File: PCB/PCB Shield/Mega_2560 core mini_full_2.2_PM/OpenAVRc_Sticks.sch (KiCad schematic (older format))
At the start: 58 parts, among them P11 Trim, P12 Stick_left, P13 Stick_right, P14 Switch, P23 Rot_1, P24 Rot_2, P25 Keys, P28 5v/3,3v manches, P31 Pot2, P32 Pot1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

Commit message: Update Shield v2.2
-Add pullup on Rx core
-Add 3D views TOP and BOTTOM
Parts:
- P12: footprint Pin_Headers:Pin_Header_Straight_2x03_Pitch2.54mm -> Mylib_v2.2:Pin_Header_Straight_2x03_Pitch2.54mm
- P13: footprint Pin_Headers:Pin_Header_Straight_1x06_Pitch2.54mm -> Mylib_v2.2:Pin_Header_Straight_2x03_Pitch2.54mm
- R11, R12, R13, R14, R24, R25, R26, R28, R29, R31, R32, R34, R35, R37: footprint Resistors_SMD:R_1206 -> Mylib_v2.2:R_1206
- U6: footprint Librairie master:SOP14 -> Mylib_v2.2:SOP14
- W1, W2, W3, W4: footprint anthoperso:TESTPT -> Mylib_v2.2:TESTPT
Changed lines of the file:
@@
 F 0 "U6" H 6100 4700 50  0000 L CNN
 F 1 "MCP6004" H 6100 4300 50  0000 L CNN
-F 2 "Librairie master:SOP14" H 6050 4600 50  0001 C CNN
+F 2 "Mylib_v2.2:SOP14" H 6050 4600 50  0001 C CNN
 F 3 "" H 6150 4700 50  0000 C CNN
 	2    6100 4500
@@
 F 0 "U6" H 9500 4750 50  0000 L CNN
 F 1 "MCP6004" H 9500 4350 50  0000 L CNN
-F 2 "Librairie master:SOP14" H 9450 4650 50  0001 C CNN
+F 2 "Mylib_v2.2:SOP14" H 9450 4650 50  0001 C CNN
 F 3 "" H 9550 4750 50  0000 C CNN
 	4    9500 4550
@@
 F 0 "U6" H 7800 4700 50  0000 L CNN
 F 1 "MCP6004" H 7800 4300 50  0000 L CNN
-F 2 "Librairie master:SOP14" H 7750 4600 50  0001 C CNN
+F 2 "Mylib_v2.2:SOP14" H 7750 4600 50  0001 C CNN
 F 3 "" H 7850 4700 50  0000 C CNN
 	3    7800 4500
@@
 F 0 "U6" H 4400 4700 50  0000 L CNN
 F 1 "MCP6004" H 4400 4300 50  0000 L CNN
-F 2 "Librairie master:SOP14" H 4350 4600 50  0001 C CNN
+F 2 "Mylib_v2.2:SOP14" H 4350 4600 50  0001 C CNN
 F 3 "" H 4450 4700 50  0000 C CNN
 	1    4400 4500
@@
 F 0 "R26" V 5030 5350 50  0000 C CNN
 F 1 "47K" V 4950 5350 50  0000 C CNN
-F 2 "Resistors_SMD:R_1206" V 4880 5350 50  0001 C CNN
+F 2 "Mylib_v2.2:R_1206" V 4880 5350 50  0001 C CNN
 F 3 "" H 4950 5350 50  0000 C CNN
 	1    4950 5350
@@
 F 0 "R28" V 5230 5350 50  0000 C CNN
 F 1 "120K" V 5150 5350 50  0000 C CNN
-F 2 "Resistors_SMD:R_1206" V 5080 5350 50  0001 C CNN
+F 2 "Mylib_v2.2:R_1206" V 5080 5350 50  0001 C CNN
 F 3 "" H 5150 5350 50  0000 C CNN
 	1    5150 5350
@@
 F 0 "R29" V 6730 5350 50  0000 C CNN
 F 1 "47K" V 6650 5350 50  0000 C CNN
-F 2 "Resistors_SMD:R_1206" V 6580 5350 50  0001 C CNN
+F 2 "Mylib_v2.2:R_1206" V 6580 5350 50  0001 C CNN
 F 3 "" H 6650 5350 50  0000 C CNN
 	1    6650 5350
@@
 F 0 "R31" V 6930 5350 50  0000 C CNN
 F 1 "120K" V 6850 5350 50  0000 C CNN
-F 2 "Resistors_SMD:R_1206" V 6780 5350 50  0001 C CNN
+F 2 "Mylib_v2.2:R_1206" V 6780 5350 50  0001 C CNN
 F 3 "" H 6850 5350 50  0000 C CNN
 	1    6850 5350
@@
 F 0 "R32" V 8430 5350 50  0000 C CNN
 F 1 "47K" V 8350 5350 50  0000 C CNN
-F 2 "Resistors_SMD:R_1206" V 8280 5350 50  0001 C CNN
+F 2 "Mylib_v2.2:R_1206" V 8280 5350 50  0001 C CNN
 F 3 "" H 8350 5350 50  0000 C CNN
 	1    8350 5350
@@
 F 0 "R34" V 8630 5350 50  0000 C CNN
 F 1 "120K" V 8550 5350 50  0000 C CNN
-F 2 "Resistors_SMD:R_1206" V 8480 5350 50  0001 C CNN
+F 2 "Mylib_v2.2:R_1206" V 8480 5350 50  0001 C CNN
 F 3 "" H 8550 5350 50  0000 C CNN
 	1    8550 5350
@@
 F 0 "R35" V 10130 5400 50  0000 C CNN
 F 1 "47K" V 10050 5400 50  0000 C CNN
-F 2 "Resistors_SMD:R_1206" V 9980 5400 50  0001 C CNN
+F 2 "Mylib_v2.2:R_1206" V 9980 5400 50  0001 C CNN
 F 3 "" H 10050 5400 50  0000 C CNN
 	1    10050 5400
@@
 F 0 "R37" V 10330 5400 50  0000 C CNN
 F 1 "120K" V 10250 5400 50  0000 C CNN
-F 2 "Resistors_SMD:R_1206" V 10180 5400 50  0001 C CNN
+F 2 "Mylib_v2.2:R_1206" V 10180 5400 50  0001 C CNN
 F 3 "" H 10250 5400 50  0000 C CNN
 	1    10250 5400
@@
 F 0 "R24" V 3630 5550 50  0000 C CNN
 F 1 "39K" V 3550 5550 50  0000 C CNN
-F 2 "Resistors_SMD:R_1206" V 3480 5550 50  0001 C CNN
+F 2 "Mylib_v2.2:R_1206" V 3480 5550 50  0001 C CNN
 F 3 "" H 3550 5550 50  0000 C CNN
 	1    3550 5550
@@
 F 0 "R25" V 4080 5250 50  0000 C CNN
 F 1 "39K" V 4000 5250 50  0000 C CNN
-F 2 "Resistors_SMD:R_1206" V 3930 5250 50  0001 C CNN
+F 2 "Mylib_v2.2:R_1206" V 3930 5250 50  0001 C CNN
 F 3 "" H 4000 5250 50  0000 C CNN
 	1    4000 5250
@@
 F 0 "W1" H 4900 4660 50  0000 C CNN
 F 1 "TEST_2P" H 4900 4530 50  0000 C CNN
-F 2 "anthoperso:TESTPT" H 4900 4600 50  0001 C CNN
+F 2 "Mylib_v2.2:TESTPT" H 4900 4600 50  0001 C CNN
 F 3 "" H 4900 4600 50  0000 C CNN
 	1    4900 4600
@@
 F 0 "W2" H 6600 4660 50  0000 C CNN
 F 1 "TEST_2P" H 6600 4530 50  0000 C CNN
-F 2 "anthoperso:TESTPT" H 6600 4600 50  0001 C CNN
+F 2 "Mylib_v2.2:TESTPT" H 6600 4600 50  0001 C CNN
 F 3 "" H 6600 4600 50  0000 C CNN
 	1    6600 4600
@@
 F 0 "W3" H 8300 4660 50  0000 C CNN
 F 1 "TEST_2P" H 8300 4530 50  0000 C CNN
-F 2 "anthoperso:TESTPT" H 8300 4600 50  0001 C CNN
+F 2 "Mylib_v2.2:TESTPT" H 8300 4600 50  0001 C CNN
 F 3 "" H 8300 4600 50  0000 C CNN
 	1    8300 4600
@@
 F 0 "W4" H 10000 4710 50  0000 C CNN
 F 1 "TEST_2P" H 10000 4580 50  0000 C CNN
-F 2 "anthoperso:TESTPT" H 10000 4650 50  0001 C CNN
+F 2 "Mylib_v2.2:TESTPT" H 10000 4650 50  0001 C CNN
 F 3 "" H 10000 4650 50  0000 C CNN
 	1    10000 4650
@@
 F 0 "R11" V 5230 4800 50  0000 C CNN
 F 1 "68K" V 5150 4800 50  0000 C CNN
-F 2 "Resistors_SMD:R_1206" V 5080 4800 50  0001 C CNN
+F 2 "Mylib_v2.2:R_1206" V 5080 4800 50  0001 C CNN
 F 3 "" H 5150 4800 50  0000 C CNN
 	1    5150 4800
@@
 F 0 "R12" V 6930 4800 50  0000 C CNN
 F 1 "68K" V 6850 4800 50  0000 C CNN
-F 2 "Resistors_SMD:R_1206" V 6780 4800 50  0001 C CNN
+F 2 "Mylib_v2.2:R_1206" V 6780 4800 50  0001 C CNN
 F 3 "" H 6850 4800 50  0000 C CNN
 	1    6850 4800
@@
 F 0 "R13" V 8630 4800 50  0000 C CNN
 F 1 "68K" V 8550 4800 50  0000 C CNN
-F 2 "Resistors_SMD:R_1206" V 8480 4800 50  0001 C CNN
+F 2 "Mylib_v2.2:R_1206" V 8480 4800 50  0001 C CNN
 F 3 "" H 8550 4800 50  0000 C CNN
 	1    8550 4800
@@
 F 0 "R14" V 10330 4900 50  0000 C CNN
 F 1 "68K" V 10250 4900 50  0000 C CNN
-F 2 "Resistors_SMD:R_1206" V 10180 4900 50  0001 C CNN
+F 2 "Mylib_v2.2:R_1206" V 10180 4900 50  0001 C CNN
 F 3 "" H 10250 4900 50  0000 C CNN
 	1    10250 4900
@@
 F 0 "P13" H 2500 4700 50  0000 C CNN
 F 1 "Stick_right" V 2600 4350 50  0000 C CNN
-F 2 "Pin_Headers:Pin_Header_Straight_1x06_Pitch2.54mm" H 2500 4350 50  0001 C CNN
+F 2 "Mylib_v2.2:Pin_Header_Straight_2x03_Pitch2.54mm" H 2500 4350 50  0001 C CNN
 F 3 "" H 2500 4350 50  0000 C CNN
 	1    2500 4350
@@
 F 0 "P12" H 1450 4700 50  0000 C CNN
 F 1 "Stick_left" V 1550 4350 50  0000 C CNN
-F 2 "Pin_Headers:Pin_Header_Straight_2x03_Pitch2.54mm" H 1450 4350 50  0001 C CNN
+F 2 "Mylib_v2.2:Pin_Header_Straight_2x03_Pitch2.54mm" H 1450 4350 50  0001 C CNN
 F 3 "" H 1450 4350 50  0000 C CNN
 	1    1450 4350

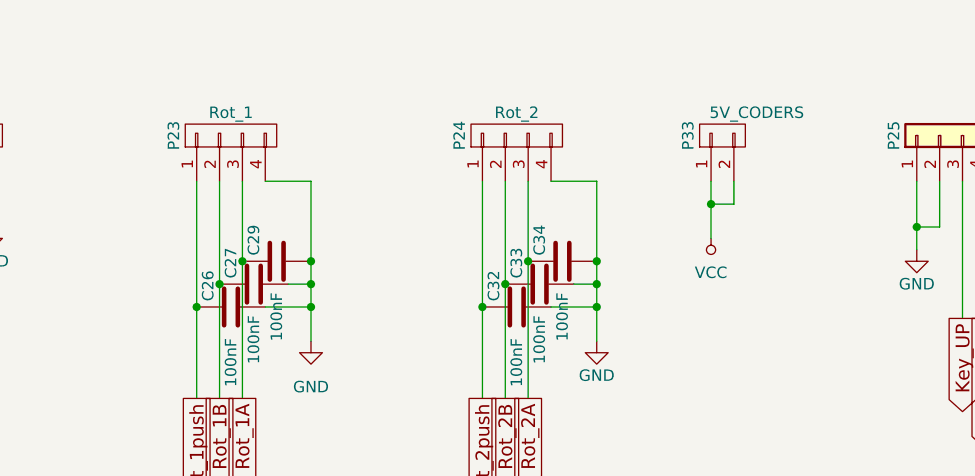
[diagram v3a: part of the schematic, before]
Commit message: Update shield v2.2
-Replace encoders connectors (add 5v)
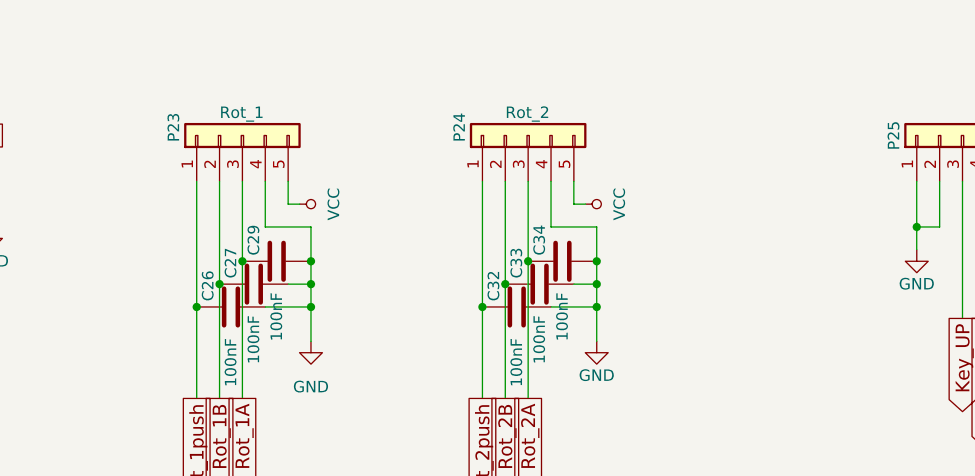
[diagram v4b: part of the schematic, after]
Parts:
- removed P23: Rot_1, Pin_Headers:Pin_Header_Straight_1x04_Pitch2.54mm, symbol Mega_2560-core-mini_full_2.2-rescue:CONN_01X04-Mega_2560-core-mini_full_2.1-Meg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
- removed P24: Rot_2, Pin_Headers:Pin_Header_Straight_1x04_Pitch2.54mm, symbol Mega_2560-core-mini_full_2.2-rescue:CONN_01X04-Mega_2560-core-mini_full_2.1-Meg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
- removed P33: 5V_CODERS, Pin_Headers:Pin_Header_Straight_1x02_Pitch2.54mm, symbol Mega_2560-core-mini_full_2.2-rescue:CONN_01X02-Mega_2560-core-mini_full_2.1-Meg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
- added P23: Rot_1, Mylib_v2.2:Pin_Header_Straight_1x05_Pitch2.54mm, symbol Connector_Generic:Conn_01x05
- added P24: Rot_2, Mylib_v2.2:Pin_Header_Straight_1x05_Pitch2.54mm, symbol Connector_Generic:Conn_01x05
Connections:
- net GND: now also P23.4 (Pin_4), P24.4 (Pin_4)
- net Rot_1A: now also P23.3 (Pin_3)
- net Rot_1B: now also P23.2 (Pin_2)
- net Rot_1push: now also P23.1 (Pin_1)
- net Rot_2A: now also P24.3 (Pin_3)
- net Rot_2B: now also P24.2 (Pin_2)
- net Rot_2push: now also P24.1 (Pin_1)
- net VCC: now also P23.5 (Pin_5), P24.5 (Pin_5)
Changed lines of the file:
@@
 Sheet 2 7
 Title "Shield Mega2560 core Full"
-Date "2020-03-07"
+Date "2020-04-03"
 Rev "2.2"
 Comp "© Team OpenAVRc"
@@
 $EndComp
 $Comp
-L Mega_2560-core-mini_full_2.2-rescue:CONN_01X04-Mega_2560-core-mini_full_2.1-Mega_2560-core-mini_full_2.1-rescue-Mega_2560-core-mini_full_2.2-rescue P23
-U 1 1 59C63F7F
-P 7050 1250
-F 0 "P23" H 7050 1500 50  0000 C CNN
-F 1 "Rot_1" V 7150 1250 50  0000 C CNN
-F 2 "Pin_Headers:Pin_Header_Straight_1x04_Pitch2.54mm" H 7050 1250 50  0001 C CNN
-F 3 "" H 7050 1250 50  0000 C CNN
-	1    7050 1250
-	0    -1   -1   0
-$EndComp
-$Comp
-L Mega_2560-core-mini_full_2.2-rescue:CONN_01X04-Mega_2560-core-mini_full_2.1-Mega_2560-core-mini_full_2.1-rescue-Mega_2560-core-mini_full_2.2-rescue P24
-U 1 1 59C63F86
-P 8300 1250
-F 0 "P24" H 8300 1500 50  0000 C CNN
-F 1 "Rot_2" V 8400 1250 50  0000 C CNN
-F 2 "Pin_Headers:Pin_Header_Straight_1x04_Pitch2.54mm" H 8300 1250 50  0001 C CNN
-F 3 "" H 8300 1250 50  0000 C CNN
-	1    8300 1250
-	0    -1   -1   0
-$EndComp
-$Comp
 L Mega_2560-core-mini_full_2.2-rescue:GND-RESCUE-Mega_2560_core_mini_full_2.0-Mega_2560-core-mini_full_2.1-rescue-Mega_2560-core-mini_full_2.1-rescue-Mega_2560-core-mini_full_2.2-rescue #PWR041
 U 1 1 59C63FC4
@@
 $EndComp
 Wire Wire Line
-	8650 1450 8650 1800
-Wire Wire Line
-	7400 1450 7400 1800
-Wire Wire Line
 	7000 1450 7000 1900
 Wire Wire Line
@@
 Wire Wire Line
 	8650 1900 8550 1900
-Wire Wire Line
-	8450 1450 8650 1450
-Connection ~ 8650 1800
 Connection ~ 8350 1800
 Connection ~ 8650 2000
@@
 Wire Wire Line
 	8350 1450 8350 1800
-Connection ~ 7400 1800
 Wire Wire Line
 	6900 1450 6900 2000
@@
 Connection ~ 8250 1900
 Wire Wire Line
-	7400 1450 7200 1450
-Wire Wire Line
 	10150 1450 10150 1650
 Wire Wire Line
@@
 	3050 5850 3050 5750
 $Comp
-L Mega_2560-core-mini_full_2.2-rescue:CONN_01X02-Mega_2560-core-mini_full_2.1-Mega_2560-core-mini_full_2.1-rescue-Mega_2560-core-mini_full_2.2-rescue P33
-U 1 1 5A71A89A
-P 9200 1250
-AR Path="/5A71A89A" Ref="P33"  Part="1"
-AR Path="/59C5A6CD/5A71A89A" Ref="P33"  Part="1"
-F 0 "P33" H 9200 1400 50  0000 C CNN
-F 1 "5V_CODERS" V 9300 1100 50  0000 C CNN
-F 2 "Pin_Headers:Pin_Header_Straight_1x02_Pitch2.54mm" H 9200 1250 50  0001 C CNN
-F 3 "" H 9200 1250 50  0000 C CNN
-	1    9200 1250
-	0    -1   -1   0
-$EndComp
-$Comp
-L Mega_2560-core-mini_full_2.2-rescue:VCC-power1 #PWR044
-U 1 1 5A71ACEB
-P 9150 1700
-F 0 "#PWR044" H 9150 1550 50  0001 C CNN
-F 1 "VCC" H 9150 1850 50  0000 C CNN
-F 2 "" H 9150 1700 50  0000 C CNN
-F 3 "" H 9150 1700 50  0000 C CNN
-	1    9150 1700
-	-1   0    0    1
-$EndComp
-Wire Wire Line
-	9150 1700 9150 1550
-Wire Wire Line
-	9150 1550 9250 1550
-Wire Wire Line
-	9250 1550 9250 1450
-Connection ~ 9150 1550
-$Comp
 L Mega_2560-core-mini_full_2.2-rescue:C-RESCUE-Mega_2560_core_mini_full_2.0-Mega_2560-core-mini_full_2.1-rescue-Mega_2560-core-mini_full_2.1-rescue-Mega_2560-core-mini_full_2.2-rescue C32
 U 1 1 5A72E2A9
@@
 	10050 1650 10050 1750
 Wire Wire Line
-	9150 1550 9150 1450
-Wire Wire Line
 	3750 5000 3550 5000
 Wire Wire Line
@@
 	0    -1   -1   0
 $EndComp
+$Comp
+L Connector_Generic:Conn_01x05 P23
+U 1 1 5E89125F
+P 7100 1250
+F 0 "P23" H 7200 1550 50  0000 R CNN
+F 1 "Rot_1" V 7200 1350 50  0000 R CNN
+F 2 "Mylib_v2.2:Pin_Header_Straight_1x05_Pitch2.54mm" H 7100 1250 50  0001 C CNN
+F 3 "~" H 7100 1250 50  0001 C CNN
+	1    7100 1250
+	0    -1   -1   0
+$EndComp
+Wire Wire Line
+	7400 1800 7400 1650
+Wire Wire Line
+	7400 1650 7200 1650
+Wire Wire Line
+	7200 1650 7200 1450
+Connection ~ 7400 1800
+$Comp
+L Mega_2560-core-mini_full_2.2-rescue:VCC-power1 #PWR0153
+U 1 1 5E8A94C4
+P 7350 1550
+F 0 "#PWR0153" H 7350 1400 50  0001 C CNN
+F 1 "VCC" H 7350 1700 50  0000 C CNN
+F 2 "" H 7350 1550 50  0000 C CNN
+F 3 "" H 7350 1550 50  0000 C CNN
+	1    7350 1550
+	0    1    1    0
+$EndComp
+Wire Wire Line
+	7350 1550 7300 1550
+Wire Wire Line
+	7300 1550 7300 1450
+$Comp
+L Connector_Generic:Conn_01x05 P24
+U 1 1 5E8C03AC
+P 8350 1250
+F 0 "P24" H 8450 1550 50  0000 R CNN
+F 1 "Rot_2" V 8450 1350 50  0000 R CNN
+F 2 "Mylib_v2.2:Pin_Header_Straight_1x05_Pitch2.54mm" H 8350 1250 50  0001 C CNN
+F 3 "~" H 8350 1250 50  0001 C CNN
+	1    8350 1250
+	0    -1   -1   0
+$EndComp
+Wire Wire Line
+	8650 1800 8650 1650
+Wire Wire Line
+	8650 1650 8450 1650
+Wire Wire Line
+	8450 1650 8450 1450
+Connection ~ 8650 1800
+$Comp
+L Mega_2560-core-mini_full_2.2-rescue:VCC-power1 #PWR0154
+U 1 1 5E8D7108
+P 8600 1550
+F 0 "#PWR0154" H 8600 1400 50  0001 C CNN
+F 1 "VCC" H 8600 1700 50  0000 C CNN
+F 2 "" H 8600 1550 50  0000 C CNN
+F 3 "" H 8600 1550 50  0000 C CNN
+	1    8600 1550
+	0    1    1    0
+$EndComp
+Wire Wire Line
+	8600 1550 8550 1550
+Wire Wire Line
+	8550 1550 8550 1450
 $EndSCHEMATC
